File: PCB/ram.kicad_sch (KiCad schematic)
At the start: 34 parts, among them SW5 SW_DIP_x08, SW6 SW_Push, U20 74LS04, U21 74189, U22 74LS04, U23 74189, U24 74LS158, U25 74LS245, U26 74LS00, U27 74LS04, U28 74LS04, U5 74LS04, U51 74LS158, U52 74LS158

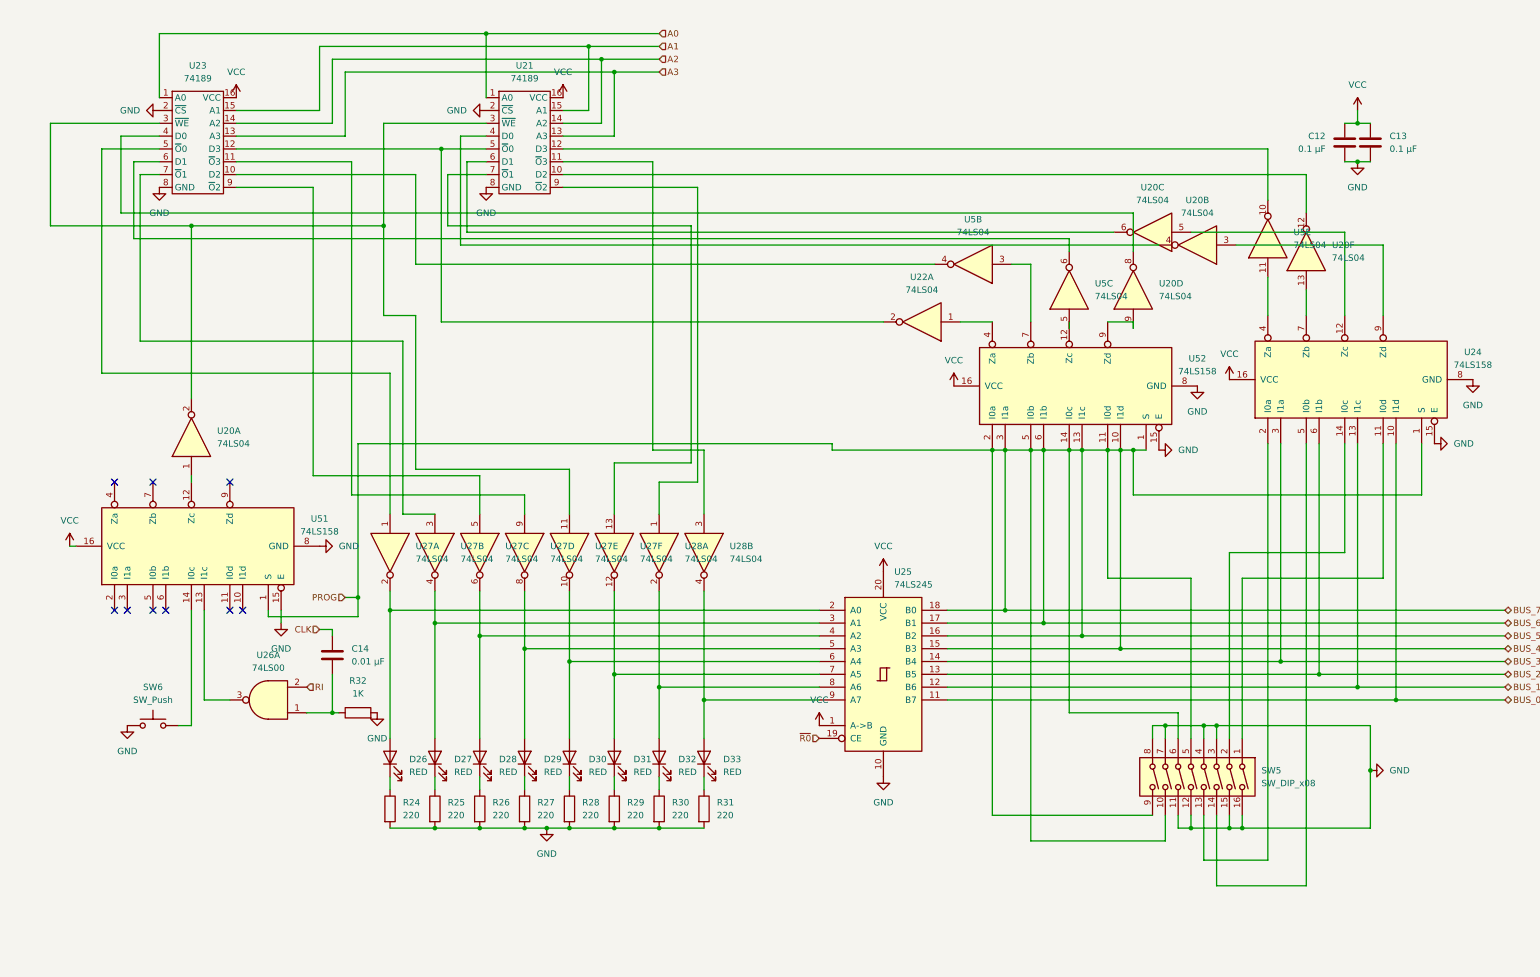
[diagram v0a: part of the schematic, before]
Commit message: Routed the traces for the ground
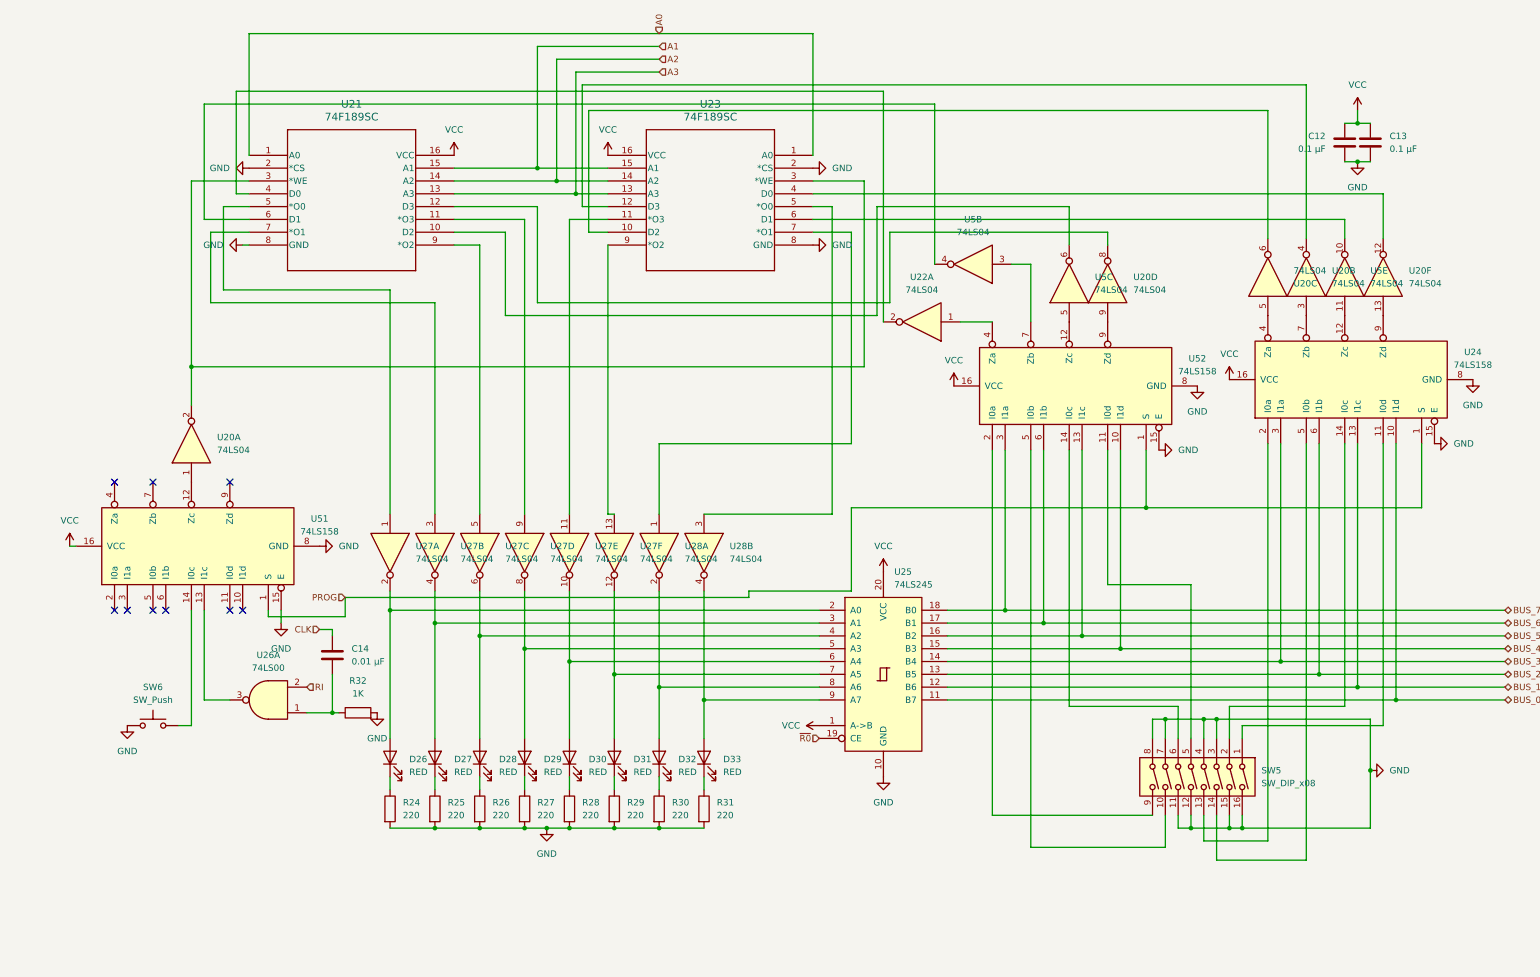
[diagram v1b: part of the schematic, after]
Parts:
- removed U21, U23: 74189, Custom:N16, symbol Custom:74F189SJ
- added U21, U23: 74F189SC, SOIC16_9P9X3P9_ONS, symbol 2025-11-05_14-44-06:74F189SC
- added unit 4 of U22
- added unit 2 of U22
- added unit 6 of U22
- added unit 5 of U22
- added unit 1 of U22
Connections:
- net A0: now also U21.1 (A0), U23.1 (A0)
- net A1: now also U21.15 (A1), U23.15 (A1)
- net A2: now also U21.14 (A2), U23.14 (A2)
- net A3: now also U21.13 (A3), U23.13 (A3)
- net BUS_4: no longer SW5.10, SW5.5, SW5.6, SW5.9, U24.1 (S), U25.16 (B2), U25.17 (B1), U25.18 (B0), U51.1 (S), U52.1 (S), U52.11 (I0d), U52.13 (I1c), U52.14 (I0c), U52.2 (I0a), U52.3 (I1a), U52.5 (I0b), U52.6 (I1b)
- net GND: now also U21.2 (*CS), U21.8 (GND), U23.2 (*CS), U23.8 (GND)
- net VCC: now also U21.16 (VCC), U23.16 (VCC)
- net at U27.3: now also U21.7 (*O1)
- net at U28.1: now also U23.7 (*O1)
- net at U52.4 (Za): now also U22.1; no longer U22.1
- net at U27.5: now also U21.9 (*O2)
- net at U5.6: now also U21.10 (D2)
- net at U20.12: now also U23.4 (D0)
- net at U28.3: now also U23.5 (*O0)
- net at U5.10: now also U23.6 (D1)
- net at U27.11: now also U23.11 (*O3); no longer U20.2
- net at U20.4: now also U23.12 (D3)
- net at U20.6: now also U23.10 (D2)
- net at U27.13: now also U23.9 (*O2)
- net at U5.4: now also U21.6 (D1)
- net at U27.9: now also U21.11 (*O3)
- net at U20.8: now also U21.12 (D3)
- net at U27.1: now also U21.5 (*O0)
- net at U20.5: now also U24.4 (Za); no longer U24.12 (Zc)
- net at U20.3: now also U24.7 (Zb); no longer U24.9 (Zd)
- net at U5.11: now also U24.12 (Zc); no longer U24.4 (Za)
- net at U20.13: now also U24.9 (Zd); no longer U24.7 (Zb)
- new net: SW5.5, U52.11 (I0d)
- new net: SW5.6, U52.14 (I0c)
- new net: SW5.9, U52.2 (I0a)
- new net: SW5.10, U52.5 (I0b)
- new net: U20.2, U21.3 (*WE), U23.3 (*WE)
- new net: U21.4 (D0), U22.2
- new net BUS_5: U25.16 (B2), U52.13 (I1c)
- new net BUS_6: U25.17 (B1), U52.6 (I1b)
- new net BUS_7: U25.18 (B0), U52.3 (I1a)
- new net PROG: U24.1 (S), U51.1 (S), U52.1 (S)
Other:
- moved on the sheet: U20A, U20B, U20C, U20D, U20F, U22C, U5C, U5E

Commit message: Add decupling caps and reroute pcb. Updated BOM to match new number of caps
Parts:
- added C37, C39, C42, C44, C45, C47, C48, C50, C51, C53: 0.1 µF, Capacitor_THT:C_Radial_D5.0mm_H5.0mm_P2.00mm, symbol Device:C
- U21, U23: footprint SOIC16_9P9X3P9_ONS -> Custom:SOIC16_9P9X3P9_ONS
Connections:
- net GND: now also C37.2, C39.2, C42.2, C44.2, C45.2, C47.2, C48.2, C50.2, C51.2, C53.2
- net VCC: now also C37.1, C39.1, C42.1, C44.1, C45.1, C47.1, C48.1, C50.1, C51.1, C53.1

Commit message: Redoing PCB layout and fixed some signal flow convention errors
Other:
- moved on the sheet: C48, C51, U22G

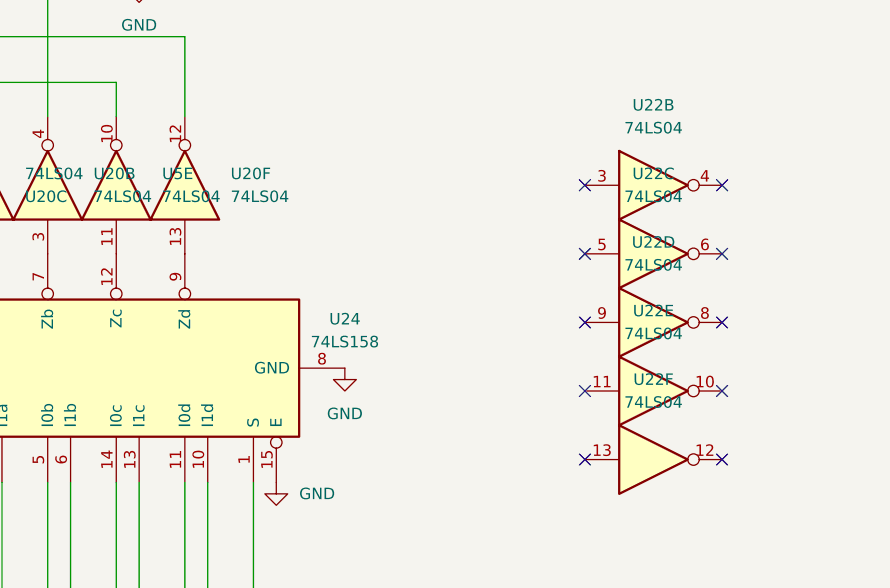
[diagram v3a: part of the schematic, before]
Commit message: update BOM to reflect cheaper prices and more acurate item ammounts, also worked on laying out the PCB.
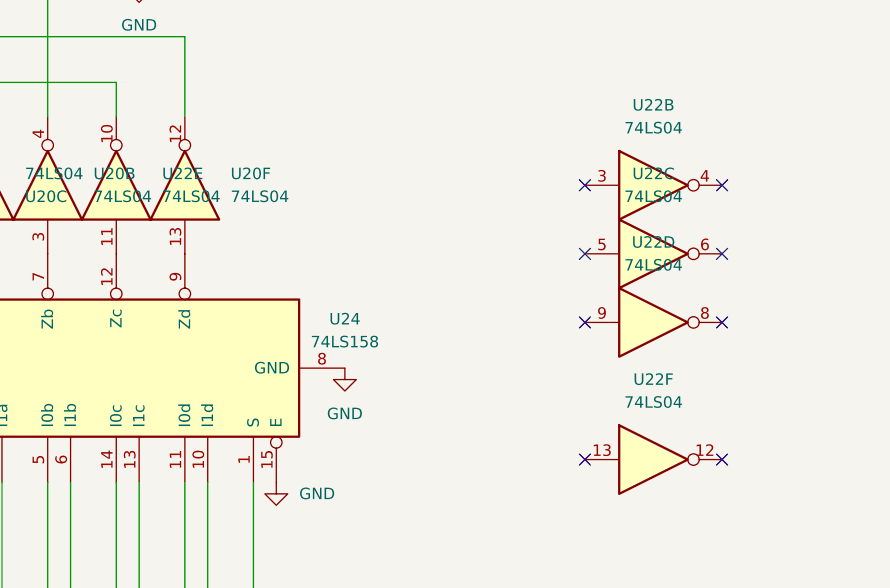
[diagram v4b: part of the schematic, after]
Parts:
- removed unit 5 of U5
- U21, U23: footprint Custom:SOIC16_9P9X3P9_ONS -> Package_DIP:DIP-16_W7.62mm
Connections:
- net at U23.6 (D1): now also U22.10
- net at U24.12 (Zc): now also U22.11
- no-connect marks 19 -> 17
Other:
- moved on the sheet: U22E
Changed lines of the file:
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@@
 	)
 	(no_connect
-		(at 327.66 87.63)
-	)
-	(no_connect
 		(at 342.9 72.39)
 	)
@@
 	)
 	(no_connect
-		(at 342.9 87.63)
-	)
-	(no_connect
 		(at 54.61 130.81)
 	)
@@
 			)
 		)
-		(property "Footprint" "Custom:SOIC16_9P9X3P9_ONS"
+		(property "Footprint" "Package_DIP:DIP-16_W7.62mm"
 			(at 170.18 40.64 0)
 			(effects
@@
 			)
 		)
-		(property "Footprint" "Custom:SOIC16_9P9X3P9_ONS"
+		(property "Footprint" "Package_DIP:DIP-16_W7.62mm"
 			(at 58.42 40.64 0)
 			(effects
@@
 	)
 	(symbol
-		(lib_id "74xx:74LS04")
-		(at 275.59 64.77 90)
-		(unit 5)
-		(exclude_from_sim no)
-		(in_bom yes)
-		(on_board yes)
-		(dnp no)
-		(fields_autoplaced yes)
-		(property "Reference" "U5"
-			(at 280.67 63.4999 90)
-			(effects
-				(font
-					(size 1.27 1.27)
-				)
-				(justify right)
-			)
-		)
-		(property "Value" "74LS04"
-			(at 280.67 66.0399 90)
-			(effects
-				(font
-					(size 1.27 1.27)
-				)
-				(justify right)
-			)
-		)
-		(property "Footprint" "Package_DIP:DIP-14_W7.62mm"
-			(at 275.59 64.77 0)
-			(effects
-				(font
-					(size 1.27 1.27)
-				)
-				(hide yes)
-			)
-		)
-		(property "Datasheet" "http://www.ti.com/lit/gpn/sn74LS04"
-			(at 275.59 64.77 0)
-			(effects
-				(font
-					(size 1.27 1.27)
-				)
-				(hide yes)
-			)
-		)
-		(property "Description" "Hex Inverter"
-			(at 275.59 64.77 0)
-			(effects
-				(font
-					(size 1.27 1.27)
-				)
-				(hide yes)
-			)
-		)
-		(pin "9"
-		)
-		(pin "6"
-		)
-		(pin "14"
-		)
-		(pin "8"
-		)
-		(pin "2"
-		)
-		(pin "12"
-		)
-		(pin "4"
-		)
-		(pin "5"
-		)
-		(pin "11"
-		)
-		(pin "13"
-		)
-		(pin "7"
-		)
-		(pin "3"
-		)
-		(pin "1"
-		)
-		(pin "10"
-		)
-		(instances
-			(project ""
-				(path "/48633dea-2de9-4b6f-aeff-2ee54233f918/fa2f47c1-e570-4190-9168-df734bfd379c"
-					(reference "U5")
-					(unit 5)
-				)
-			)
-		)
-	)
-	(symbol
 		(lib_id "power:GND")
 		(at 58.42 43.18 0)
@@
 	(symbol
 		(lib_id "74xx:74LS04")
-		(at 335.28 87.63 0)
+		(at 275.59 64.77 90)
 		(unit 5)
 		(exclude_from_sim no)
@@
 		(fields_autoplaced yes)
 		(property "Reference" "U22"
-			(at 335.28 78.74 0)
+			(at 280.67 63.4999 90)
 			(effects
 				(font
 					(size 1.27 1.27)
 				)
+				(justify right)
 			)
 		)
 		(property "Value" "74LS04"
-			(at 335.28 81.28 0)
+			(at 280.67 66.0399 90)
 			(effects
 				(font
 					(size 1.27 1.27)
 				)
+				(justify right)
 			)
 		)
 		(property "Footprint" "Package_DIP:DIP-14_W7.62mm"
-			(at 335.28 87.63 0)
+			(at 275.59 64.77 0)
 			(effects
 				(font
@@
 		)
 		(property "Datasheet" "http://www.ti.com/lit/gpn/sn74LS04"
-			(at 335.28 87.63 0)
+			(at 275.59 64.77 0)
 			(effects
 				(font
@@
 		)
 		(property "Description" "Hex Inverter"
-			(at 335.28 87.63 0)
+			(at 275.59 64.77 0)
 			(effects
 				(font
